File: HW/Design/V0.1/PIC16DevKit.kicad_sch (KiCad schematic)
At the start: 0 parts

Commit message: Update diagram
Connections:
- no-connect marks 34 -> 35
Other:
- sheet POWER ports: added VBUS_DIV, VDDTG_DIV, VPP_DIV; removed VBUS_SEN
- sheet PROGRAMMER ports: added VBUS_DET, VDDTG_SEN, VPP_SEN, ~{BT_FNC}; removed USB_VBUS

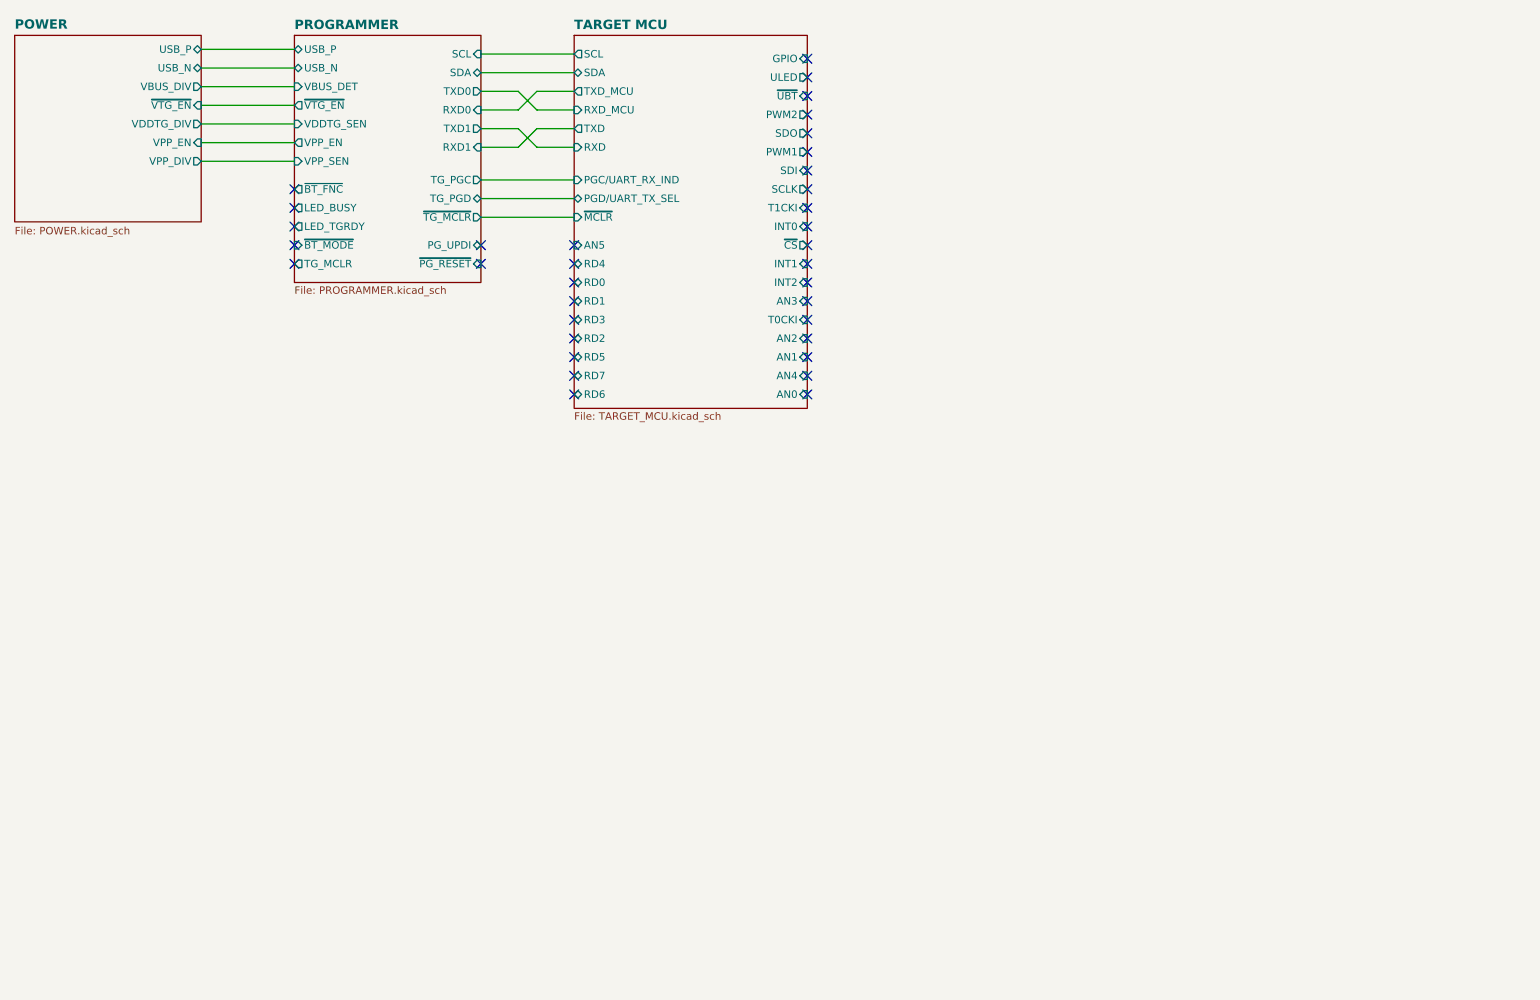
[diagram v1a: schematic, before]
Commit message: AVR64DU28 bootloader update 2
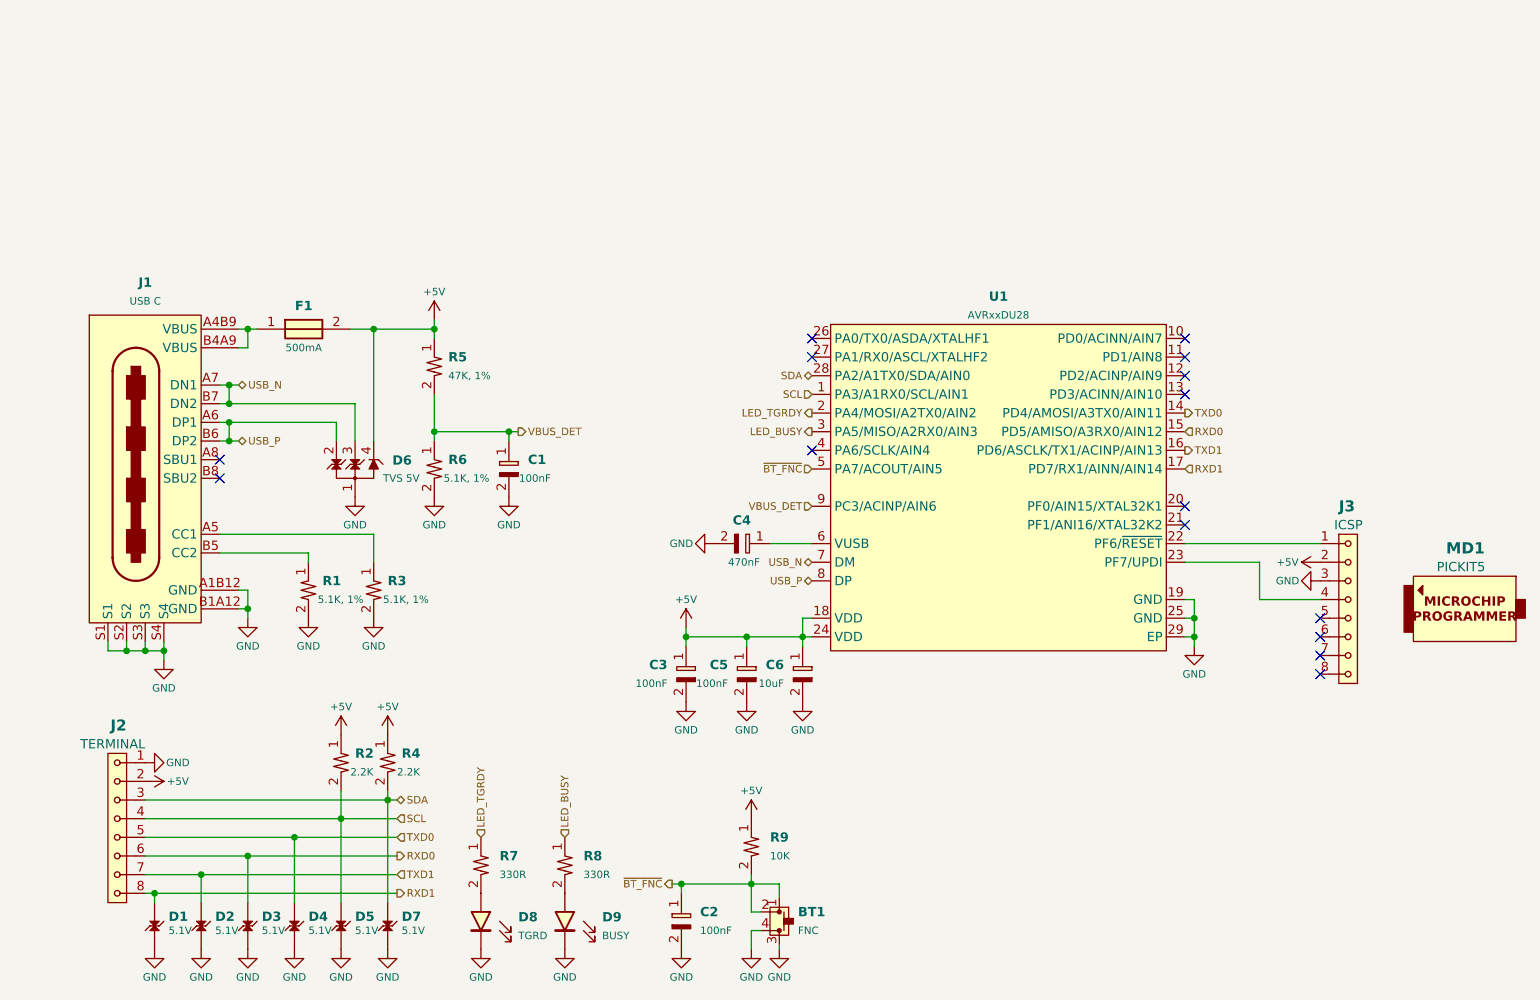
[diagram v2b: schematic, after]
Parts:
- added BT1: FNC, Liem:SW6x6-G, symbol SAMPI:BT2
- added C1, C2, C3, C5: 100nF, SAMPI:CAP0603, symbol Triet_KiCAD_Sym:CAP_CER
- added C4: 470nF, SAMPI:CAP0603, symbol Triet_KiCAD_Sym:CAP_CER
- added C6: 10uF, SAMPI:CAP0603, symbol Triet_KiCAD_Sym:CAP_CER
- added D1, D2, D3, D4, D5, D7: 5.1V, Liem:SOD-323_12, symbol SAMPI:TVS
- added D6: TVS 5V, SAMPI:SOT143B_NEXT, symbol SAMPI:TVS_3CH
- added D8: TGRD, SAMPI:LED0603, symbol Triet_KiCAD_Sym:LED
- added D9: BUSY, SAMPI:LED0603, symbol Triet_KiCAD_Sym:LED
- added F1: 500mA, SAMPI:FUSE1812, symbol Triet_KiCAD_Sym:Fuse
- added J1: USB C, SAMPI:USB4105, symbol SAMPI:USB4105
- added J2: TERMINAL, symbol SAMPI:SIL08
- added J3: ICSP, symbol SAMPI:SIL08
- added MD1: PICKIT5, symbol SAMPI:SNAP-PG164100
- added R1, R3, R6: 5.1K, 1%, SAMPI:RES0603, symbol Triet_KiCAD_Sym:RES
- added R2, R4: 2.2K, SAMPI:RES0603, symbol Triet_KiCAD_Sym:RES
- added R5: 47K, 1%, SAMPI:RES0603, symbol Triet_KiCAD_Sym:RES
- added R7, R8: 330R, SAMPI:RES0603, symbol Triet_KiCAD_Sym:RES
- added R9: 10K, SAMPI:RES0603, symbol Triet_KiCAD_Sym:RES
- added U1: AVRxxDU28, SAMPI:VQFN28-4x4-EP, symbol SAMPI:AVRxxDU28
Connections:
- new net: D9.A, R8.2
- new net: C4.1, U1.6 (VUSB)
- new net: J1.B5 (CC2), R1.1
- new net: J1.A5 (CC1), R3.1
- new net: J3.1, U1.22 (PF6/~{RESET})
- new net: J3.4, U1.23 (PF7/UPDI)
- new net: D8.A, R7.2
- new net: F1.1, J1.A4B9 (VBUS), J1.B4A9 (VBUS)
- new net +5V: C3.1, C5.1, C6.1, D6.4 (CH3), F1.2, J2.2, J3.2, R2.1, R4.1, R5.1, R9.1, U1.18 (VDD), U1.24 (VDD)
- new net GND: BT1.3, BT1.4, C1.2, C2.2, C3.2, C4.2, C5.2, C6.2, D1.2, D2.2, D3.2, D4.2, D5.2, D6.1 (GND), D7.2, D8.K, D9.K, J1.A1B12 (GND), J1.B1A12 (GND), J1.S1, J1.S2, J1.S3, J1.S4, J2.1, J3.3, R1.2, R3.2, R6.2, U1.19 (GND), U1.25 (GND), U1.29 (EP)
- new net LED_BUSY: R8.1, U1.3 (PA5/MISO/A2RX0/AIN3)
- new net LED_TGRDY: R7.1, U1.2 (PA4/MOSI/A2TX0/AIN2)
- new net RXD0: D3.1, J2.6, U1.15 (PD5/AMISO/A3RX0/AIN12)
- new net RXD1: D1.1, J2.8, U1.17 (PD7/RX1/AINN/AIN14)
- new net SCL: D5.1, J2.4, R2.2, U1.1 (PA3/A1RX0/SCL/AIN1)
- new net SDA: D7.1, J2.3, R4.2, U1.28 (PA2/A1TX0/SDA/AIN0)
- new net TXD0: D4.1, J2.5, U1.14 (PD4/AMOSI/A3TX0/AIN11)
- new net TXD1: D2.1, J2.7, U1.16 (PD6/ASCLK/TX1/ACINP/AIN13)
- new net USB_N: D6.3 (CH2), J1.A7 (DN1), J1.B7 (DN2), U1.7 (DM)
- new net USB_P: D6.2 (CH1), J1.A6 (DP1), J1.B6 (DP2), U1.8 (DP)
- new net VBUS_DET: C1.1, R5.2, R6.1, U1.9 (PC3/ACINP/AIN6)
- new net ~{BT_FNC}: BT1.1, BT1.2, C2.1, R9.2, U1.5 (PA7/ACOUT/AIN5)
- no-connect marks 35 -> 15
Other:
- removed sheet POWER
- removed sheet PROGRAMMER
- removed sheet TARGET MCU
- company: SAMPI DEVELOPMENT KITS -> (none)
- title: PIC16F877A DEV KIT -> USB TO DUAL SERIAL PORT & I2C CONVERTER
